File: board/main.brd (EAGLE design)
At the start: 32.7 x 83.8 mm, 58 parts, among them IC1 ATMEGA48/88/168-AU, IC2 LM386N-1, J1 AVR_SPI_PRG_6PTH, Q2 MOSFET-NCHANNELSMD, Q3 MOSFET-NCHANNELSMD, U1 AT24C1024B-8S2, U2 AT24C1024B-8S2

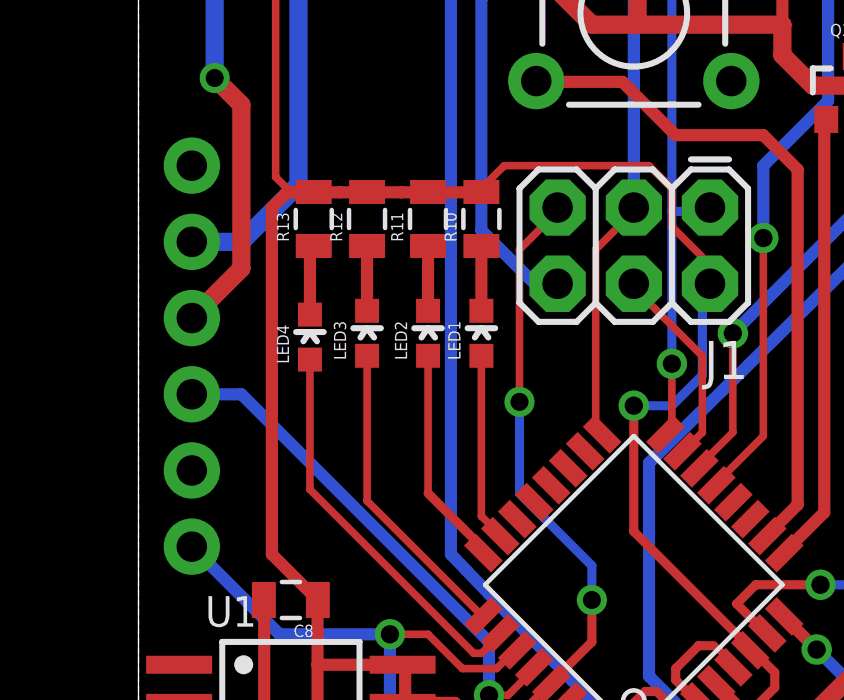
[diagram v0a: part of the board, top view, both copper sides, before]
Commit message: Fixed the TWI interface
Seems there was a problem with the waiting for-i2c-logic.  Fixed and now it's working.  Yippie.  SO MUCH WASTED TIME.  Ugh.
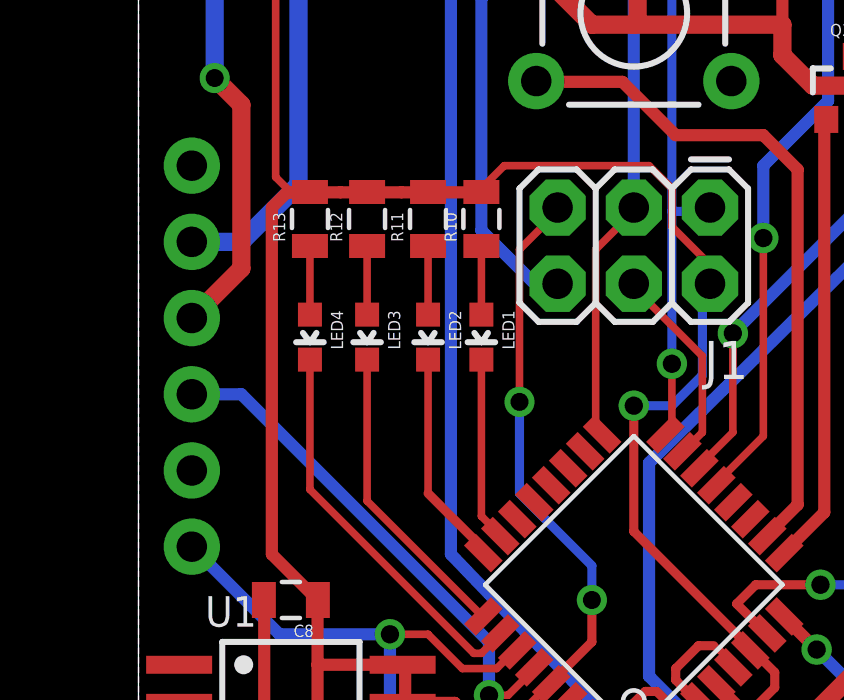
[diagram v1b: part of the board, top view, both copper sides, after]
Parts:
- R10, R11, R12, R13: value 150 -> 330
- moved LED1 0.13 mm to (11.4, 28.6), turned to 180 degrees
- moved LED2 0.13 mm to (9.65, 28.6), turned to 180 degrees
- moved LED3 0.13 mm to (7.62, 28.6), turned to 180 degrees
- moved R13 0.13 mm to (5.71, 32.5)
- turned LED4 to 180 degrees
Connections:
- net LED1: now also LED1.C; no longer LED1.A
- net LED2: now also LED2.C; no longer LED2.A
- net LED3: now also LED3.C; no longer LED3.A
- net LED4: now also LED4.C; no longer LED4.A
- net N$10: now also LED1.A, R10.1; no longer LED4.C, R13.1
- net N$11: now also LED2.A, R11.1; no longer LED3.C, R12.1
- net N$13: now also LED3.A, R12.1; no longer LED2.C, R11.1
- net N$14: now also LED4.A, R13.1; no longer LED1.C, R10.1
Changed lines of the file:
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@@
 <?xml version="1.0" encoding="utf-8"?>
 <!DOCTYPE eagle SYSTEM "eagle.dtd">
-<eagle version="6.2">
+<eagle version="7.2.0">
 <drawing>
 <settings>
@@
 <setting verticaltext="up"/>
 </settings>
-<grid distance="0.05" unitdist="inch" unit="inch" style="lines" multiple="1" display="yes" altdistance="0.005" altunitdist="inch" altunit="inch"/>
+<grid distance="0.025" unitdist="inch" unit="inch" style="lines" multiple="1" display="yes" altdistance="0.005" altunitdist="inch" altunit="inch"/>
 <layers>
 <layer number="1" name="Top" color="4" fill="1" visible="yes" active="yes"/>
@@
 </class>
 </classes>
-<designrules>
+<designrules name="default">
 <description language="de">&lt;b&gt;EAGLE Design Rules&lt;/b&gt;
 &lt;p&gt;
@@
 <pass name="Default">
 <param name="RoutingGrid" value="10mil"/>
+<param name="AutoGrid" value="1"/>
+<param name="Efforts" value="0"/>
+<param name="TopRouterVariant" value="1"/>
 <param name="tpViaShape" value="octagon"/>
 <param name="PrefDir.1" value="*"/>
@@
 <element name="C9" library="SparkFun" package="0805" value="" x="8.255" y="42.291" rot="R270"/>
 <element name="JP4" library="SparkFun" package="1X04" value="" x="27.305" y="26.67" rot="R90"/>
-<element name="LED1" library="SparkFun" package="LED-0603" value="" x="11.43" y="28.702"/>
-<element name="LED2" library="SparkFun" package="LED-0603" value="" x="9.652" y="28.702"/>
-<element name="LED3" library="SparkFun" package="LED-0603" value="" x="7.62" y="28.702"/>
-<element name="R10" library="SparkFun" package="0805" value="150" x="11.43" y="32.512" rot="R90"/>
-<element name="R11" library="SparkFun" package="0805" value="150" x="9.652" y="32.512" rot="R90"/>
-<element name="R12" library="SparkFun" package="0805" value="150" x="7.62" y="32.512" rot="R90"/>
-<element name="LED4" library="SparkFun" package="LED-0603" value="" x="5.715" y="28.575"/>
-<element name="R13" library="SparkFun" package="0805" value="150" x="5.842" y="32.512" rot="R90"/>
+<element name="LED1" library="SparkFun" package="LED-0603" value="" x="11.43" y="28.575" rot="R180"/>
+<element name="LED2" library="SparkFun" package="LED-0603" value="" x="9.652" y="28.575" rot="R180"/>
+<element name="LED3" library="SparkFun" package="LED-0603" value="" x="7.62" y="28.575" rot="R180"/>
+<element name="R10" library="SparkFun" package="0805" value="330" x="11.43" y="32.512" rot="R90"/>
+<element name="R11" library="SparkFun" package="0805" value="330" x="9.652" y="32.512" rot="R90"/>
+<element name="R12" library="SparkFun" package="0805" value="330" x="7.62" y="32.512" rot="R90"/>
+<element name="LED4" library="SparkFun" package="LED-0603" value="" x="5.715" y="28.575" rot="R180"/>
+<element name="R13" library="SparkFun" package="0805" value="330" x="5.715" y="32.512" rot="R90"/>
 <element name="Q3" library="SparkFun" package="SOT23-3" value="MOSFET-NCHANNELSMD" x="23.876" y="36.83"/>
 <element name="S1" library="SparkFun" package="TACTILE-PTH" value="SWITCH-MOMENTARY-2PTH" x="16.51" y="39.37"/>
@@
 <signal name="LED1">
 <contactref element="IC1" pad="23"/>
-<contactref element="LED1" pad="A"/>
-<wire x1="11.43" y1="22.606" x2="11.43" y2="27.952" width="0.254" layer="1"/>
 <wire x1="11.938" y1="22.098" x2="11.43" y2="22.606" width="0.254" layer="1"/>
 <wire x1="11.938" y1="22.098" x2="12.060459375" y2="21.9411125" width="0.254" layer="1"/>
+<contactref element="LED1" pad="C"/>
+<wire x1="11.43" y1="22.606" x2="11.43" y2="27.825" width="0.254" layer="1"/>
 </signal>
 <signal name="LED2">
 <contactref element="IC1" pad="24"/>
-<contactref element="LED2" pad="A"/>
-<wire x1="9.652" y1="23.368" x2="9.652" y2="27.952" width="0.254" layer="1"/>
 <wire x1="11.43" y1="21.59" x2="9.652" y2="23.368" width="0.3048" layer="1"/>
 <wire x1="11.43" y1="21.59" x2="11.494771875" y2="21.375425" width="0.254" layer="1"/>
+<contactref element="LED2" pad="C"/>
+<wire x1="9.652" y1="23.368" x2="9.652" y2="27.825" width="0.254" layer="1"/>
 </signal>
 <signal name="LED3">
 <contactref element="IC1" pad="25"/>
-<contactref element="LED3" pad="A"/>
-<wire x1="7.62" y1="23.114" x2="7.62" y2="27.952" width="0.254" layer="1"/>
 <wire x1="11.43" y1="19.304" x2="7.62" y2="23.114" width="0.254" layer="1"/>
 <wire x1="11.43" y1="19.304" x2="11.494771875" y2="19.264571875" width="0.254" layer="1"/>
+<contactref element="LED3" pad="C"/>
+<wire x1="7.62" y1="23.114" x2="7.62" y2="27.825" width="0.254" layer="1"/>
 </signal>
 <signal name="LED4">
 <contactref element="IC1" pad="26"/>
-<contactref element="LED4" pad="A"/>
-<wire x1="5.715" y1="23.495" x2="5.715" y2="27.825" width="0.254" layer="1"/>
 <wire x1="11.176" y1="18.034" x2="5.715" y2="23.495" width="0.254" layer="1"/>
 <wire x1="11.43" y1="18.034" x2="11.176" y2="18.034" width="0.254" layer="1"/>
 <wire x1="11.938" y1="18.542" x2="11.43" y2="18.034" width="0.254" layer="1"/>
 <wire x1="11.938" y1="18.542" x2="12.060459375" y2="18.698884375" width="0.254" layer="1"/>
-</signal>
-<signal name="N$10">
-<contactref element="R13" pad="1"/>
 <contactref element="LED4" pad="C"/>
-<wire x1="5.715" y1="31.369" x2="5.715" y2="29.337" width="0.4064" layer="1"/>
-<wire x1="5.715" y1="29.337" x2="5.715" y2="29.325" width="0.254" layer="1"/>
-<wire x1="5.715" y1="31.369" x2="5.842" y2="31.612" width="0.254" layer="1"/>
-</signal>
-<signal name="N$11">
-<contactref element="R12" pad="1"/>
-<contactref element="LED3" pad="C"/>
-<wire x1="7.62" y1="31.612" x2="7.62" y2="29.452" width="0.4064" layer="1"/>
-</signal>
-<signal name="N$13">
-<contactref element="R11" pad="1"/>
-<contactref element="LED2" pad="C"/>
-<wire x1="9.652" y1="31.496" x2="9.652" y2="29.464" width="0.4064" layer="1"/>
-<wire x1="9.652" y1="29.464" x2="9.652" y2="29.452" width="0.254" layer="1"/>
-<wire x1="9.652" y1="31.496" x2="9.652" y2="31.612" width="0.254" layer="1"/>
-</signal>
-<signal name="N$14">
-<contactref element="R10" pad="1"/>
-<contactref element="LED1" pad="C"/>
-<wire x1="11.43" y1="31.612" x2="11.43" y2="29.452" width="0.4064" layer="1"/>
+<wire x1="5.715" y1="27.825" x2="5.715" y2="23.495" width="0.254" layer="1"/>
 </signal>
 <signal name="NCL_PWR">
@@
 <wire x1="4.445" y1="21.336" x2="4.445" y2="32.893" width="0.4064" layer="1"/>
 <wire x1="5.969" y1="19.812" x2="4.445" y2="21.336" width="0.4064" layer="1"/>
-<wire x1="4.953" y1="33.401" x2="5.842" y2="33.412" width="0.4064" layer="1"/>
+<wire x1="4.953" y1="33.401" x2="5.715" y2="33.412" width="0.4064" layer="1"/>
 <wire x1="5.969" y1="19.812" x2="5.98" y2="19.812" width="0.4064" layer="1"/>
 <wire x1="19.05" y1="30.988" x2="19.05" y2="30.353" width="0.254" layer="1"/>
@@
 <wire x1="4.572" y1="41.275" x2="5.588" y2="42.291" width="0.254" layer="1"/>
 <wire x1="4.572" y1="33.909" x2="5.08" y2="33.401" width="0.254" layer="1"/>
-<wire x1="5.08" y1="33.401" x2="5.842" y2="33.412" width="0.254" layer="1"/>
+<wire x1="5.08" y1="33.401" x2="5.715" y2="33.412" width="0.254" layer="1"/>
 <contactref element="IC1" pad="6"/>
 <contactref element="IC1" pad="4"/>
@@
 </polygon>
 </signal>
+<signal name="N$10">
+<contactref element="R10" pad="1"/>
+<contactref element="LED1" pad="A"/>
+<wire x1="11.43" y1="29.325" x2="11.43" y2="31.612" width="0.254" layer="1"/>
+</signal>
+<signal name="N$11">
+<contactref element="R11" pad="1"/>
+<contactref element="LED2" pad="A"/>
+<wire x1="9.652" y1="29.325" x2="9.652" y2="31.612" width="0.254" layer="1"/>
+</signal>
+<signal name="N$13">
+<contactref element="R12" pad="1"/>
+<contactref element="LED3" pad="A"/>
+<wire x1="7.62" y1="29.325" x2="7.62" y2="31.612" width="0.254" layer="1"/>
+</signal>
+<signal name="N$14">
+<contactref element="R13" pad="1"/>
+<contactref element="LED4" pad="A"/>
+<wire x1="5.715" y1="29.325" x2="5.715" y2="31.612" width="0.254" layer="1"/>
+</signal>
 </signals>
